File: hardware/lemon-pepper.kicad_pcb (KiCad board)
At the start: 4 copper layers, 35 x 35 mm, 78 parts, among them J101 INPUT, J201 USB_C_Receptacle_USB2.0, J301 TagConnect, M101 MOT, Q501 MMBT5551, U201 SRV05-4, U301 STM32G431, U302 SN65HVD230, U401 MT6835, U501 MAX15062CATA+T, U601 L6226QTR, U701 ACS711KEXLT-15AB-T, U702 ACS711KEXLT-15AB-T, U703 ACS711KEXLT-15AB-T, Y301 12MHz

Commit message: fix bringup issues
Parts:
- added R401: 10k, Resistor_SMD:R_0402_1005Metric, F.Cu at (147.5, 91.8)
- moved C502 0.11 mm to (157.8, 94.8)
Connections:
- U501 pad 6: Net-(U501-VCC) -> unconnected-(U501-~{RESET}-Pad6)
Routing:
- net +3V3: track 61.5 -> 68.6 mm
- net GND: track 97.7 -> 93.8 mm
- net Net-(U501-VCC): track 3.37 -> 5.97 mm
- net /encoder/COPI: track 24.1 -> 23.4 mm
- net /encoder/SCK: track 25.5 -> 24.9 mm
- net /encoder/CIPO: track 22.4 -> 21.7 mm

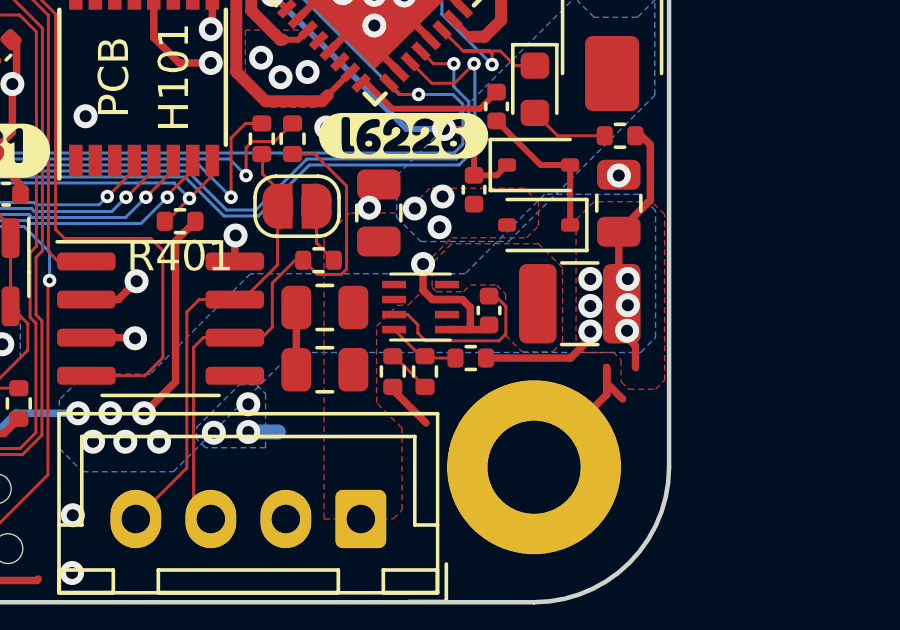
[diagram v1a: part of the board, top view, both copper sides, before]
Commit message: remove stray files/folders
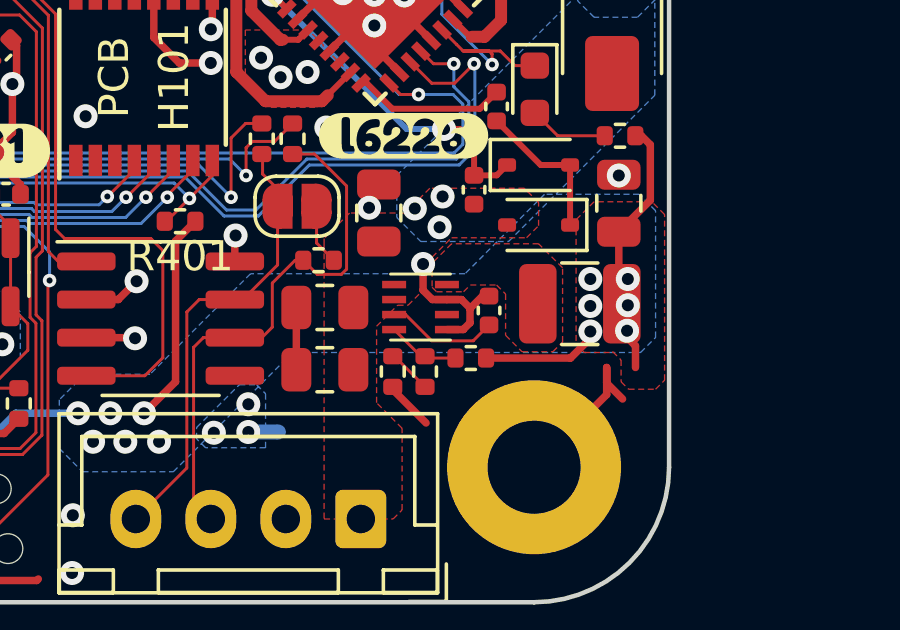
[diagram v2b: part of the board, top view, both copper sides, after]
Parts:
- turned C502 to 90 degrees
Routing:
- net Net-(U501-VCC): track 5.97 -> 3.75 mm
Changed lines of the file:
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@@
   )
   (footprint "Capacitor_SMD:C_0402_1005Metric" (layer "F.Cu")
-    (at 157.8 94.75 -90)
+    (at 157.8 94.75 90)
     (descr "Capacitor SMD 0402 (1005 Metric), square (rectangular) end terminal, IPC_7351 nominal, (Body size source: IPC-SM-782 page 76, https://www.pcb-3d.com/wordpress/wp-content/uploads/ipc-sm-782a_amendment_1_and_2.pdf), generated with kicad-footprint-generator")
     (tags "capacitor")
@@
     (fp_line (start 0.5 0.25) (end -0.5 0.25)
       (stroke (width 0.1) (type solid)) (layer "F.Fab"))
-    (pad "1" smd roundrect (at -0.48 0 270) (size 0.56 0.62) (layers "F.Cu" "F.Paste" "F.Mask") (roundrect_rratio 0.25)
+    (pad "1" smd roundrect (at -0.48 0 90) (size 0.56 0.62) (layers "F.Cu" "F.Paste" "F.Mask") (roundrect_rratio 0.25)
       (net 13 "Net-(U501-VCC)") (pintype "passive"))
-    (pad "2" smd roundrect (at 0.48 0 270) (size 0.56 0.62) (layers "F.Cu" "F.Paste" "F.Mask") (roundrect_rratio 0.25)
+    (pad "2" smd roundrect (at 0.48 0 90) (size 0.56 0.62) (layers "F.Cu" "F.Paste" "F.Mask") (roundrect_rratio 0.25)
       (net 1 "GND") (pintype "passive"))
     (model "${KICAD6_3DMODEL_DIR}/Capacitor_SMD.3dshapes/C_0402_1005Metric.wrl"
@@
   (segment (start 137.075 75.85) (end 137.075 74.8) (width 0.25) (layer "F.Cu") (net 1))
   (segment (start 131.075 92.075) (end 130.275 91.275) (width 0.25) (layer "F.Cu") (net 1))
-  (segment (start 157.175 95.385) (end 156.395 95.385) (width 0.25) (layer "F.Cu") (net 1))
-  (segment (start 156.395 94.385) (end 156.91 94.385) (width 0.25) (layer "F.Cu") (net 1))
   (segment (start 153.975 84.225) (end 154 84.225) (width 0.25) (layer "F.Cu") (net 1))
   (segment (start 136.721898 79.028102) (end 136.721898 77.721898) (width 0.25) (layer "F.Cu") (net 1))
@@
   (segment (start 147.474157 86.499157) (end 146.625 85.65) (width 0.25) (layer "F.Cu") (net 1))
   (segment (start 154 82.825) (end 154 84.225) (width 0.25) (layer "F.Cu") (net 1))
+  (segment (start 156.87962 94.385) (end 157.165 94.67038) (width 0.25) (layer "F.Cu") (net 1))
   (segment (start 153.975 86.025) (end 153.975 85.967767) (width 0.25) (layer "F.Cu") (net 1))
   (segment (start 153.95 82.775) (end 154 82.825) (width 0.25) (layer "F.Cu") (net 1))
   (segment (start 147.31538 82.95) (end 147.42 82.95) (width 0.25) (layer "F.Cu") (net 1))
   (segment (start 132.95 91.9) (end 133.935589 90.914411) (width 0.25) (layer "F.Cu") (net 1))
-  (segment (start 156.91 94.385) (end 157.175 94.65) (width 0.25) (layer "F.Cu") (net 1))
   (segment (start 153.303553 83.175) (end 154 83.871447) (width 0.25) (layer "F.Cu") (net 1))
   (segment (start 140.5 98.85) (end 141.635 98.85) (width 0.25) (layer "F.Cu") (net 1))
@@
   (segment (start 134.535913 94.860913) (end 133.842948 95.553878) (width 0.25) (layer "F.Cu") (net 1))
   (segment (start 153.3 83.175) (end 153.303553 83.175) (width 0.25) (layer "F.Cu") (net 1))
+  (segment (start 157.165 94.67038) (end 157.165 94.685) (width 0.25) (layer "F.Cu") (net 1))
   (segment (start 153.179756 81.636989) (end 154 82.457233) (width 0.25) (layer "F.Cu") (net 1))
+  (segment (start 157.165 94.685) (end 157.58 94.27) (width 0.25) (layer "F.Cu") (net 1))
   (segment (start 146.625 84.2) (end 146.625 83.64038) (width 0.25) (layer "F.Cu") (net 1))
   (segment (start 141.910438 87.201525) (end 142.05 87.061963) (width 0.25) (layer "F.Cu") (net 1))
@@
   (segment (start 136.721898 77.721898) (end 136.525 77.525) (width 0.25) (layer "F.Cu") (net 1))
   (segment (start 142.775 103.7) (end 142.725 103.75) (width 0.25) (layer "F.Cu") (net 1))
+  (segment (start 156.94 95.385) (end 157.165 95.16) (width 0.25) (layer "F.Cu") (net 1))
   (segment (start 156.474874 84.225) (end 155.525 84.225) (width 0.25) (layer "F.Cu") (net 1))
   (segment (start 149.35 92.2495) (end 149.325 92.2745) (width 0.25) (layer "F.Cu") (net 1))
@@
   (segment (start 141.596766 89.128234) (end 141.596766 89.971766) (width 0.25) (layer "F.Cu") (net 1))
   (segment (start 156.234457 83.051203) (end 155.06066 84.225) (width 0.25) (layer "F.Cu") (net 1))
+  (segment (start 157.165 95.16) (end 157.165 94.685) (width 0.25) (layer "F.Cu") (net 1))
   (segment (start 140.44283 102.94283) (end 140.44283 102.556006) (width 0.25) (layer "F.Cu") (net 1))
   (segment (start 136.675 79.075) (end 136.721898 79.028102) (width 0.25) (layer "F.Cu") (net 1))
   (segment (start 156.395 94.385) (end 155.91038 94.385) (width 0.25) (layer "F.Cu") (net 1))
+  (segment (start 156.395 94.385) (end 156.87962 94.385) (width 0.25) (layer "F.Cu") (net 1))
   (segment (start 139.591726 97.583274) (end 140.27762 96.89738) (width 0.25) (layer "F.Cu") (net 1))
   (segment (start 155.173797 81.990543) (end 154 83.16434) (width 0.25) (layer "F.Cu") (net 1))
@@
   (segment (start 131.760589 88.739411) (end 130.714411 88.739411) (width 0.25) (layer "F.Cu") (net 1))
   (segment (start 161.72 96.65) (end 161.72 97.555) (width 0.25) (layer "F.Cu") (net 1))
-  (segment (start 157.8495 95.385) (end 157.175 95.385) (width 0.25) (layer "F.Cu") (net 1))
   (segment (start 139.907035 99.442965) (end 140.5 98.85) (width 0.25) (layer "F.Cu") (net 1))
   (segment (start 154 85.992767) (end 154 85.8) (width 0.25) (layer "F.Cu") (net 1))
@@
   (segment (start 152.232233 84.225) (end 152.575 84.225) (width 0.25) (layer "F.Cu") (net 1))
   (segment (start 145.44 94.385) (end 144.375 94.385) (width 0.25) (layer "F.Cu") (net 1))
-  (segment (start 157.175 94.65) (end 157.175 95.385) (width 0.25) (layer "F.Cu") (net 1))
   (segment (start 156.941564 83.75831) (end 156.474874 84.225) (width 0.25) (layer "F.Cu") (net 1))
   (segment (start 146.625 85.65) (end 146.625 84.2) (width 0.25) (layer "F.Cu") (net 1))
@@
   (segment (start 156.588011 83.404756) (end 155.767767 84.225) (width 0.25) (layer "F.Cu") (net 1))
   (segment (start 142.725 103.75) (end 141.25 103.75) (width 0.25) (layer "F.Cu") (net 1))
+  (segment (start 156.395 95.385) (end 156.94 95.385) (width 0.25) (layer "F.Cu") (net 1))
   (segment (start 141.25 103.75) (end 140.44283 102.94283) (width 0.25) (layer "F.Cu") (net 1))
   (segment (start 152.472649 82.344096) (end 153.3 83.171447) (width 0.25) (layer "F.Cu") (net 1))
@@
   (segment (start 136.388533 93.008293) (end 136.883507 93.008293) (width 0.25) (layer "F.Cu") (net 1))
   (segment (start 132.85 92.225) (end 132.7 92.075) (width 0.25) (layer "F.Cu") (net 1))
+  (segment (start 157.58 94.27) (end 157.8 94.27) (width 0.25) (layer "F.Cu") (net 1))
   (segment (start 154 85.8) (end 153.975 85.775) (width 0.25) (layer "F.Cu") (net 1))
   (segment (start 151.411989 83.404756) (end 152.232233 84.225) (width 0.25) (layer "F.Cu") (net 1))
@@
   (segment (start 151.43934 85.725) (end 150.925 85.725) (width 0.2) (layer "F.Cu") (net 11))
   (segment (start 147.05 79.732106) (end 149.875 82.557106) (width 0.4) (layer "F.Cu") (net 11))
-  (segment (start 158.36 94.61) (end 158.02 94.27) (width 0.1) (layer "F.Cu") (net 13))
-  (segment (start 158.02 94.27) (end 157.8 94.27) (width 0.1) (layer "F.Cu") (net 13))
-  (segment (start 158.131544 95.76) (end 158.36 95.531544) (width 0.1) (layer "F.Cu") (net 13))
-  (segment (start 155.425 95.5) (end 155.685 95.76) (width 0.1) (layer "F.Cu") (net 13))
-  (segment (start 155.085 94.885) (end 155.425 95.225) (width 0.1) (layer "F.Cu") (net 13))
-  (segment (start 158.36 95.531544) (end 158.36 94.61) (width 0.1) (layer "F.Cu") (net 13))
-  (segment (start 154.635 94.885) (end 155.085 94.885) (width 0.1) (layer "F.Cu") (net 13))
-  (segment (start 155.685 95.76) (end 158.131544 95.76) (width 0.1) (layer "F.Cu") (net 13))
-  (segment (start 155.425 95.225) (end 155.425 95.5) (width 0.1) (layer "F.Cu") (net 13))
+  (segment (start 157.27 95.76) (end 157.8 95.23) (width 0.1) (layer "F.Cu") (net 13))
+  (segment (start 155.891446 95.76) (end 157.27 95.76) (width 0.1) (layer "F.Cu") (net 13))
+  (segment (start 154.635 94.885) (end 155.016446 94.885) (width 0.1) (layer "F.Cu") (net 13))
+  (segment (start 155.016446 94.885) (end 155.891446 95.76) (width 0.1) (layer "F.Cu") (net 13))
   (segment (start 160.5 91.9) (end 160.5 89.9) (width 0.2) (layer "F.Cu") (net 14))
   (segment (start 159.52 89.9) (end 160.5 89.9) (width 0.2) (layer "F.Cu") (net 14))

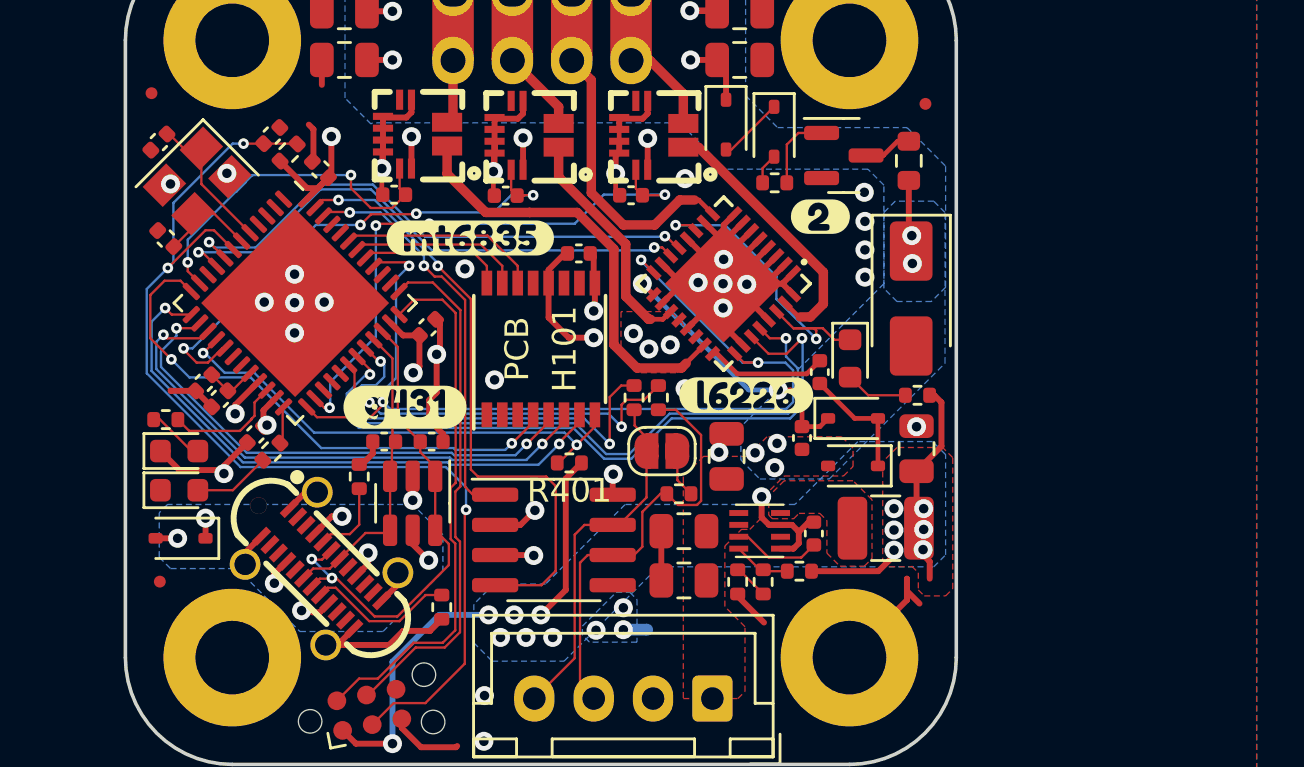
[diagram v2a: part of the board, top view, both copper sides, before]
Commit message: start working on current sense
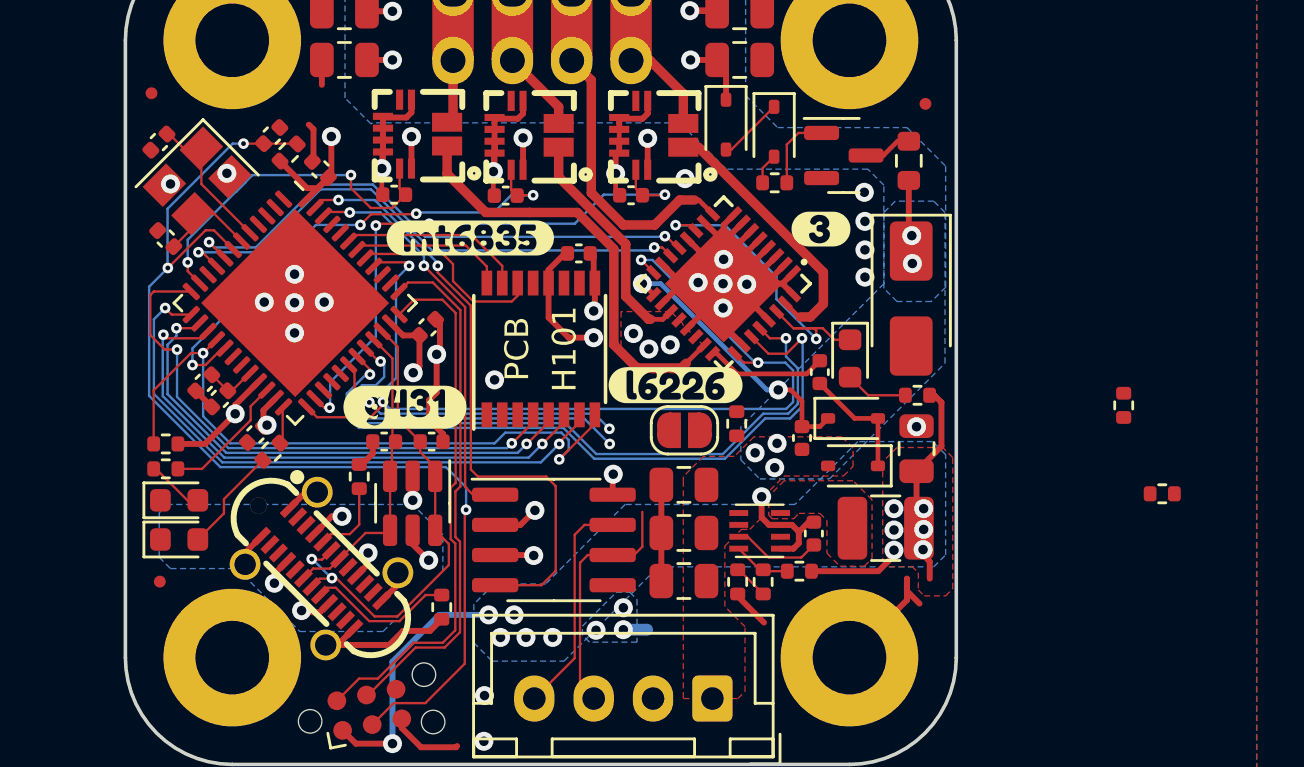
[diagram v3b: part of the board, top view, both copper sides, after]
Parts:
- removed D201: 1N4148WS, Diode_SMD:D_SOD-323
- removed kibuzzard-65380501: G***, kibuzzard-65380501
- added kibuzzard-6547C3FC: G***, kibuzzard-6547C3FC, F.Cu at (158.1, 81.9)
- moved R105 22.6 mm to (172.5, 93.1), turned to 0 degrees
- moved R104 19.6 mm to (170.8, 89.3)
- moved R401 17.0 mm to (130.5, 91.0)
- moved R103 3.83 mm to (154.6, 90.1), turned to 90 degrees
- moved kibuzzard-65305A5A 3.01 mm to (152.0, 88.5)
- moved C106 2.16 mm to (152.3, 92.7), turned to 180 degrees
- moved D302 2.08 mm to (131.1, 95.0)
- moved R301 2.08 mm to (130.5, 92.0)
- moved D301 2.07 mm to (131.1, 93.3)
- moved JP101 1.29 mm to (152.3, 90.4)
- moved C108 0.07 mm to (152.3, 94.7)
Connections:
- U301 pad 41: /encoder/A -> /encoder/Z
- U301 pad 42: /encoder/B -> /encoder/A
- U301 pad 43: /encoder/Z -> /encoder/B
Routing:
- net Vmot: track 43.2 -> 12.8 mm, vias 15 -> 14
- net /mcu/CANL: track 18.4 -> 10.3 mm
- net /encoder/CS: track 20.9 -> 28.1 mm
- net /mcu/CANH: track 15.2 -> 9.65 mm
- net GND: track 93.8 -> 88.9 mm, vias 31 -> 27
- net +3V3: track 68.6 -> 64.4 mm, vias 22 -> 21
- net /mcu/DIR: track 15.9 -> 12.6 mm
- net /mcu/STEP: track 23.6 -> 20.4 mm
- net Net-(JP101-B): track 2.04 -> 0.00 mm
- net Net-(D302-A): track 3.26 -> 4.47 mm
- net /usb/USB_5V: track 7.56 -> 6.63 mm, vias 6 -> 5
- net /encoder/CAL_EN: track 22.9 -> 23.5 mm
- net /encoder/B: track 7.30 -> 7.84 mm

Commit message: bringup changes
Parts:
- JP101: footprint Jumper:SolderJumper-2_P1.3mm_Open_RoundedPad1.0x1.5mm -> Resistor_SMD:R_0402_1005Metric
- moved R105 22.3 mm to (150.2, 91.0)
- moved R104 20.6 mm to (150.2, 90.0), turned to 180 degrees
- moved R103 2.38 mm to (152.2, 90.0), turned to 0 degrees
- moved kibuzzard-65305A5A 1.86 mm to (153.8, 88.7)
- moved JP101 0.67 mm to (152.2, 91.0)
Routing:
- net GND: track 88.9 -> 97.1 mm, vias 27 -> 28
- net /mcu/CANH: track 9.65 -> 16.7 mm
- net /mcu/CANL: track 10.3 -> 16.5 mm
- net /mcu/DIR: track 12.6 -> 14.4 mm
- net /mcu/STEP: track 20.4 -> 22.0 mm
- net /half bridges/IN1A: track 29.6 -> 31.0 mm
- net /half bridges/IN2A: track 28.7 -> 30.0 mm
- net /encoder/CAL_EN: track 23.5 -> 24.9 mm
- net /encoder/CIPO: track 21.9 -> 23.1 mm
- net /encoder/COPI: track 23.6 -> 24.8 mm
- net /mcu/RESET: track 45.9 -> 47.1 mm
- net /encoder/SCK: track 25.2 -> 26.3 mm
- net Net-(JP101-B): track 0.00 -> 1.08 mm
- net Net-(D302-A): track 4.47 -> 4.99 mm
- net +3V3: track 64.4 -> 64.5 mm, vias 21 -> 20
